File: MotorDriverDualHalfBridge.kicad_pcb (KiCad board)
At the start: 2 copper layers, 90 x 80 mm, 42 parts, among them J1 Motor Middle Connection, J2 Motor Bottom Connection, J3 Motor Upper Connection, J4 Batt+, J5 Batt-, J6 Conn_01x04, J7 Conn_01x04, Q1 IAUA250N04S6N005, Q2 IAUA250N04S6N005, U1 2ED21824S06J, U2 EL817, U3 EL817

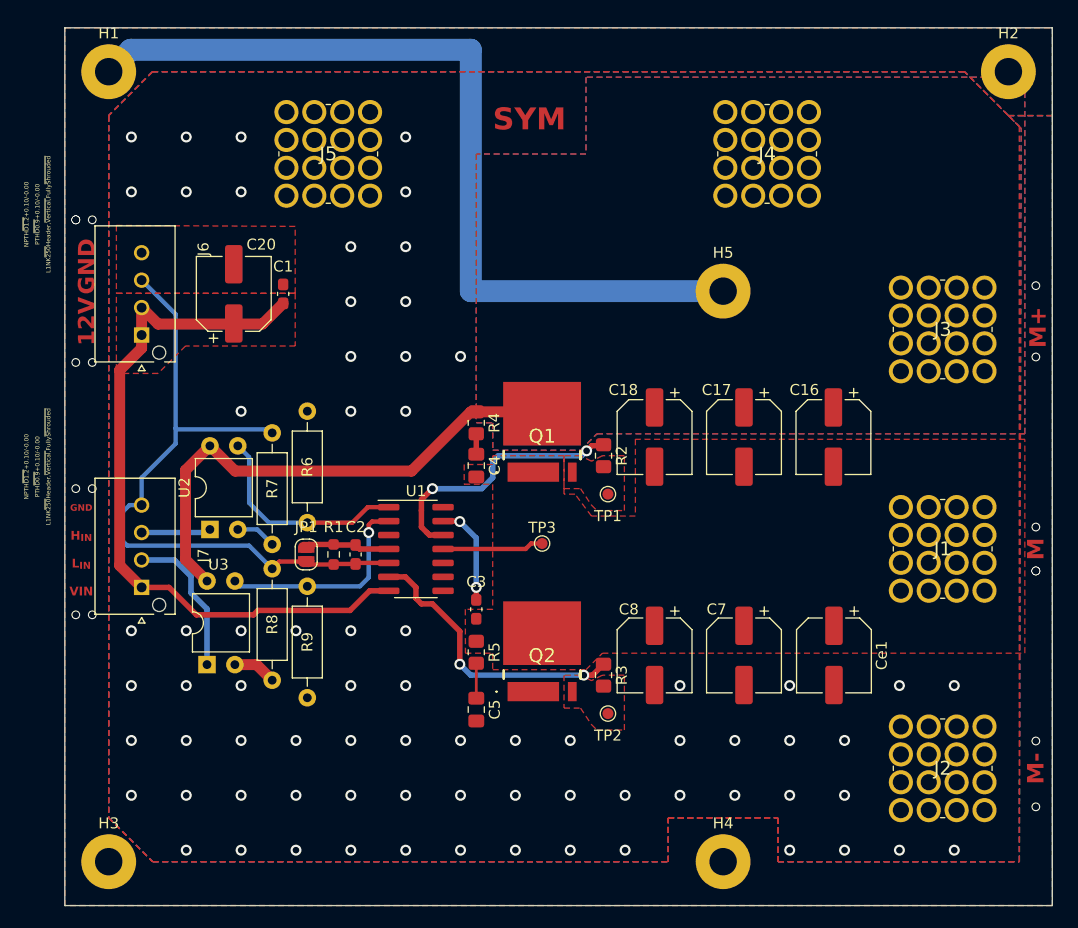
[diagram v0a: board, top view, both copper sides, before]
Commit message: Fixed traces under connectors
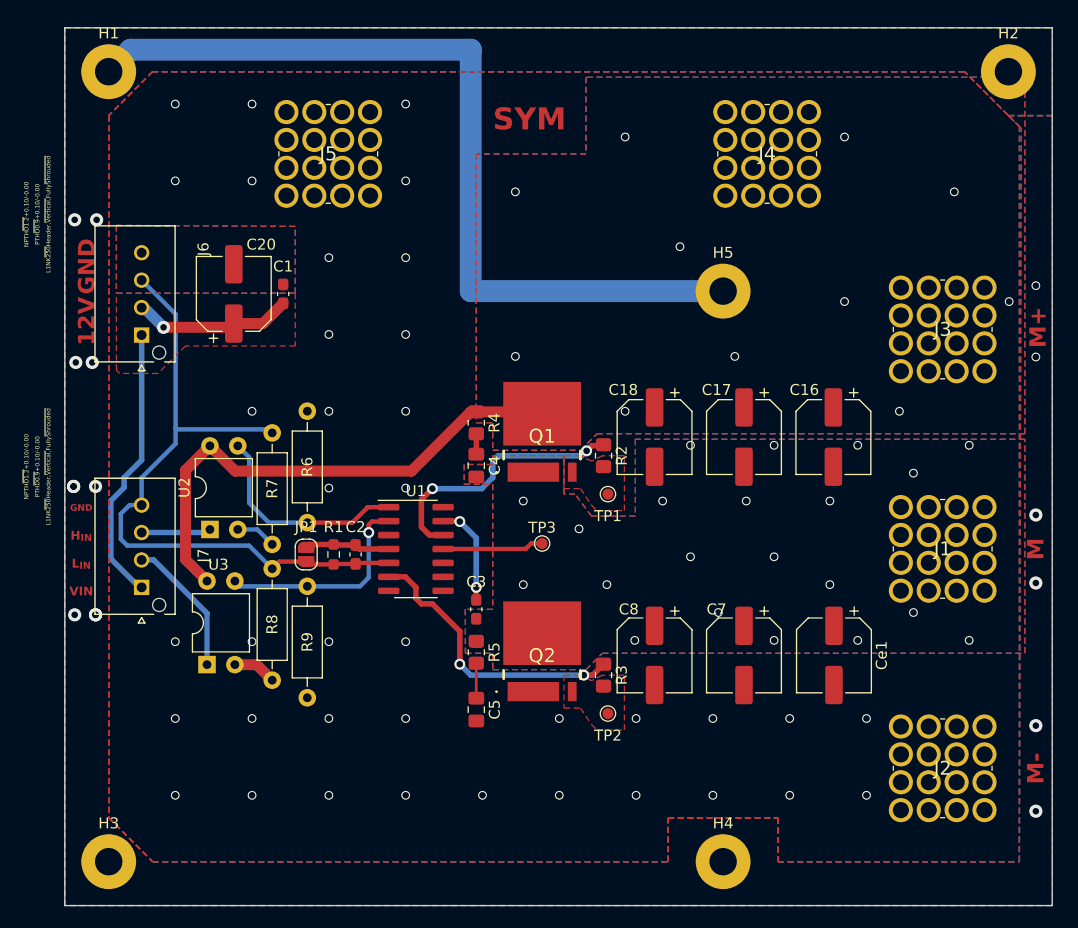
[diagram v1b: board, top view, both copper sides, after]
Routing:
- net +12V: track 65.9 -> 40.0 mm, vias 0 -> 1
- net L_{IN}: track 13.8 -> 12.7 mm
- net GNDPWR: vias 73 -> 38
- net /LOAD: vias 0 -> 21
- net +BATT: vias 0 -> 11
- added copper zone on B.Cu, net /LOAD
- added copper zone on B.Cu, net GND

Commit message: Motor Driver V1.1
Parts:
- removed C20: 100uF, Capacitor_SMD:CP_Elec_6.3x5.4_Nichicon
- removed J6: Conn_01x04, Library:MOLEX_2078430004_L1NK_250_4-PIN
- removed R6, R7, R8, R9: R_{DT}, Resistor_THT:R_Axial_DIN0207_L6.3mm_D2.5mm_P10.16mm_Horizontal
- removed U3: EL817, Package_DIP:DIP-4_W7.62mm
- added C6: 100uF, Capacitor_SMD:C_Elec_5x5.8, F.Cu at (135.9, 82.5)
- added Ce2: C_{SNUBH}, Capacitor_SMD:C_0805_2012Metric_Pad1.18x1.45mm_HandSolder, F.Cu at (159.5, 75.0)
- added Ce3: C_{SNUBL}, Capacitor_SMD:C_0805_2012Metric_Pad1.18x1.45mm_HandSolder, F.Cu at (159.5, 95.7)
- added R10: R_{DT}, Resistor_THT:R_Axial_DIN0207_L6.3mm_D2.5mm_P10.16mm_Horizontal, F.Cu at (145.5, 65.1)
- added Re1: R_{SNUBL}, Resistor_SMD:R_0805_2012Metric_Pad1.20x1.40mm_HandSolder, F.Cu at (159.5, 91.8)
- added U4: LM358, Package_DIP:DIP-8_W7.62mm_LongPads, F.Cu at (148.7, 74.0)
- added U5: EL817, Package_DIP:DIP-4_W7.62mm, F.Cu at (139.7, 74.1)
- C4: value C_{SNUBH} -> 22uF; footprint Capacitor_SMD:C_0805_2012Metric_Pad1.18x1.45mm_HandSolder -> Capacitor_SMD:CP_Elec_5x5.8
- C5: value C_{SNUBL} -> 0.1uF; footprint Capacitor_SMD:C_0805_2012Metric_Pad1.18x1.45mm_HandSolder -> Capacitor_SMD:C_0603_1608Metric_Pad1.08x0.95mm_HandSolder
- J7: value Conn_01x04 -> Conn_01x02; footprint Library:MOLEX_2078430004_L1NK_250_4-PIN -> Connector_JST:JST_EH_B2B-EH-A_1x02_P2.50mm_Vertical
- R5: value R_{SNUBL} -> 1.8k; footprint Resistor_SMD:R_0805_2012Metric_Pad1.20x1.40mm_HandSolder -> Resistor_THT:R_Axial_DIN0207_L6.3mm_D2.5mm_P10.16mm_Horizontal
- U2: value EL817 -> ~; footprint Package_DIP:DIP-4_W7.62mm -> Library:I3A4W005A150V001R
- moved C1 28.3 mm to (149.1, 86.6)
- moved C4 19.6 mm to (151.3, 92.7)
- moved R5 19.1 mm to (149.9, 108.5), turned to 90 degrees
- moved U2 11.0 mm to (130.7, 90.7), turned to 0 degrees
- moved J7 9.31 mm to (129.4, 76.7)
- moved C5 6.25 mm to (155.1, 92.7)
- moved C2 0.62 mm to (149.1, 83.1)
- moved JP1 0.62 mm to (144.6, 83.1)
- moved R1 0.62 mm to (147.1, 83.1)
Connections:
- C1 pad 2: GND -> GNDPWR
- C2 pad 2: GND -> GNDPWR
- C4 pad 1: Net-(C4-Pad1) -> +12V
- C4 pad 2: /LOAD -> GNDPWR
- C5 pad 1: Net-(C5-Pad1) -> +12V
- J7 pad 1: +12V -> /MotorDrive +
- J7 pad 2: L_{IN} -> /MotorDriver -
- JP1 pad 1: GND -> GNDPWR
- R1 pad 2: GND -> GNDPWR
- R4 pad 2: Net-(C4-Pad1) -> Net-(Ce2-Pad1)
- R5 pad 1: /LOAD -> GNDPWR
- R5 pad 2: Net-(C5-Pad1) -> Net-(U2-TRIM)
- U1 pad 1: H_{IN}_{_ISO} -> /H_{IN}
- U1 pad 2: L_{IN}_{_ISO} -> /L_{IN}
- U1 pad 5: GND -> GNDPWR
- U2 pad 1: H_{IN} -> +BATT
- U2 pad 2: Net-(R7-Pad1) -> GNDPWR
- U2 pad 3: H_{IN}_{_ISO} -> GNDPWR
- U2 pad 4: +BATT -> GNDPWR
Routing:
- net +BATT: track 47.6 -> 111.6 mm, vias 11 -> 37
- net GND: track 63.1 -> 0.00 mm
- net Net-(U4A--): track 0.00 -> 26.5 mm
- net H_{IN}_{_ISO}: track 19.7 -> 0.00 mm
- net L_{IN}_{_ISO}: track 19.5 -> 0.00 mm, vias 1 -> 0
- net /L_{IN}: track 0.00 -> 19.1 mm
- net /MotorDriver -: track 0.00 -> 15.6 mm
- net L_{IN}: track 12.7 -> 0.00 mm
- net /MotorDrive +: track 0.00 -> 12.2 mm
- net GNDPWR: track 0.00 -> 8.89 mm, vias 38 -> 26
- net /H_{IN}: track 0.00 -> 7.09 mm
- net H_{IN}: track 6.34 -> 0.00 mm
- net Net-(U2-TRIM): track 0.00 -> 5.66 mm
- net Net-(R8-Pad1): track 3.99 -> 0.00 mm
- net Net-(R7-Pad1): track 3.70 -> 0.00 mm
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- added copper zone on B.Cu, net +12V
- removed copper zone on B.Cu, net GND
- removed copper zone on F.Cu, net GND
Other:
- board text added: "+"
- board text added: "-"
- board text added: "SEM"
- board text removed: "12V"
- board text removed: "GND"
- board text removed: "H_{IN}"
- board text removed: "L_{IN}"
- board text removed: "SYM"
- board text removed: "VIN"
